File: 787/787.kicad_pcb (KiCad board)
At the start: 2 copper layers, 59.2 x 62.7 mm, 1 part

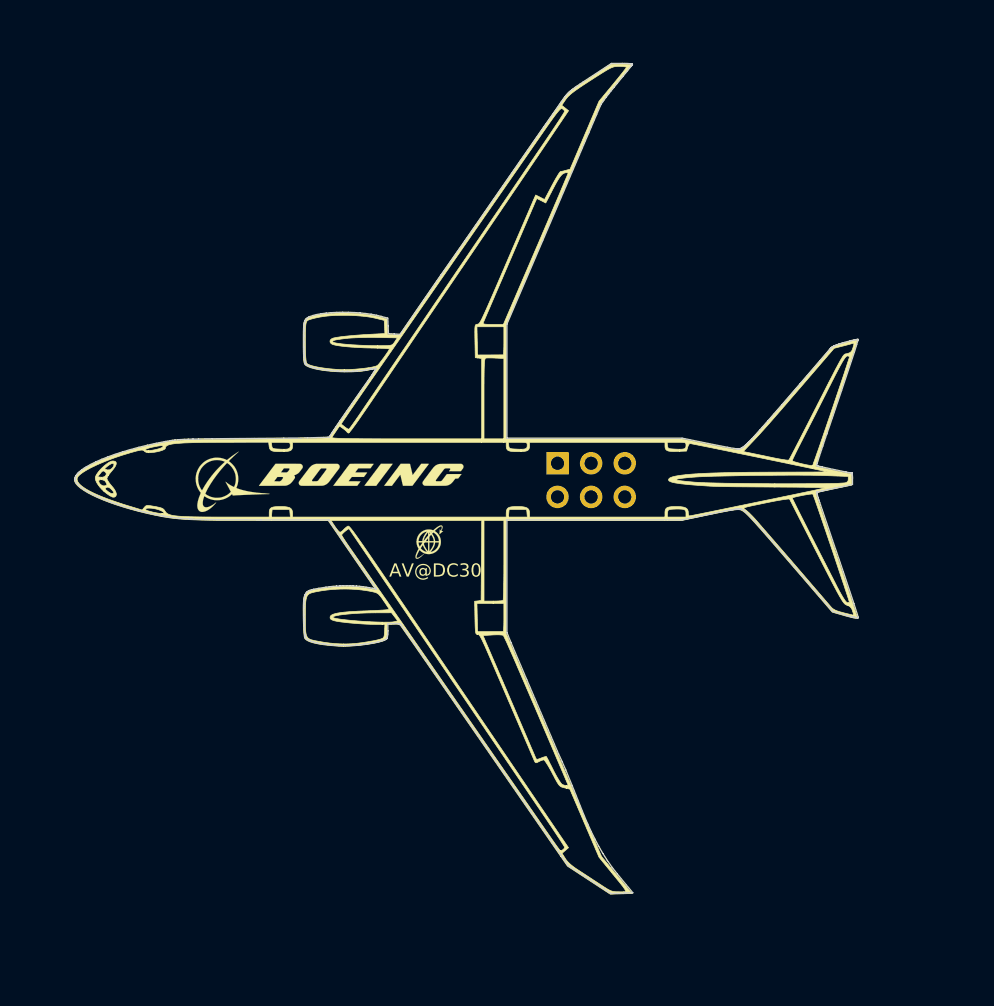
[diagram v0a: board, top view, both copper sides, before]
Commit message: updated 787 SAO version without Boeing logo
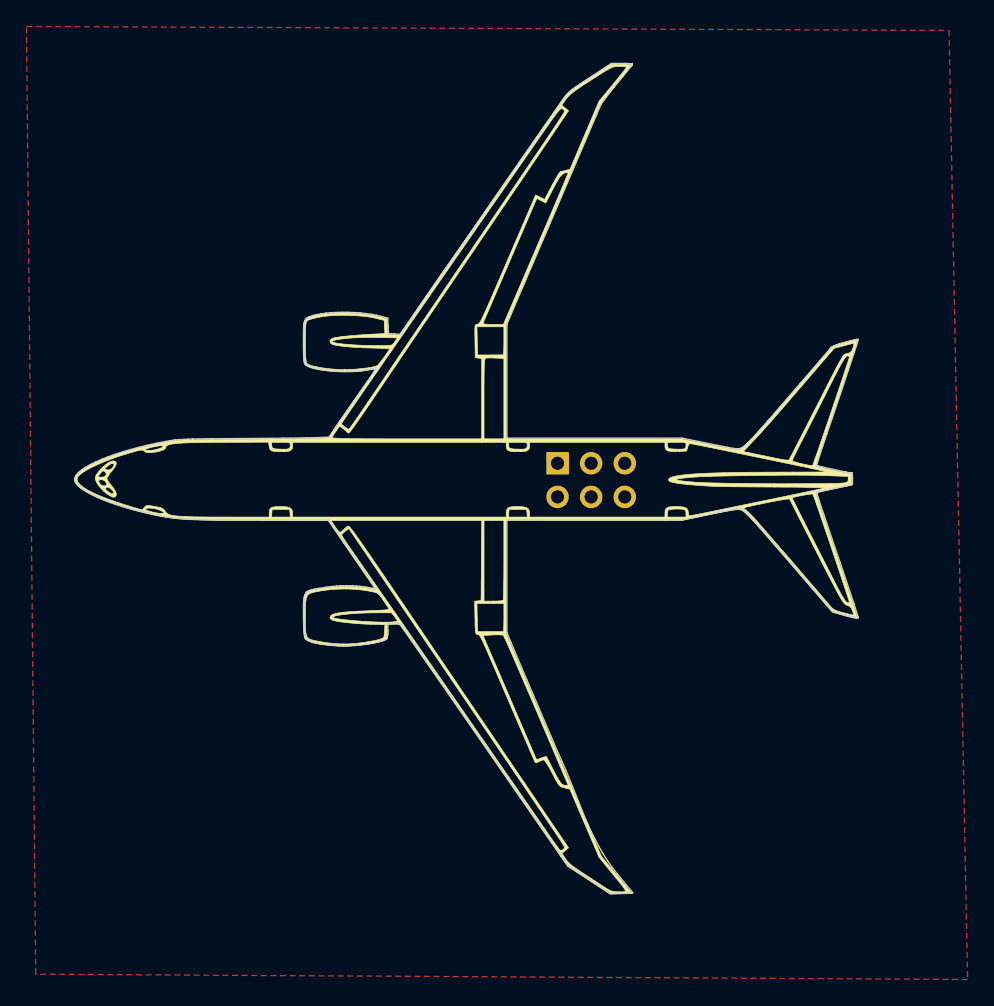
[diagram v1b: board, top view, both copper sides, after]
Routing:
- added copper zone on F.Cu, net (none)
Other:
- board text added: "@av_pubs 787 v1"
- board text added: "jlcjlcjlcjlc"
- board text removed: "AV@DC30"
